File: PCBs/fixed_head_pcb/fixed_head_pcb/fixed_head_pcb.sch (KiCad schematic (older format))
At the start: 2 parts, among them J1 DB15_Female_HighDensity, U1 Pick_and_place_pcb

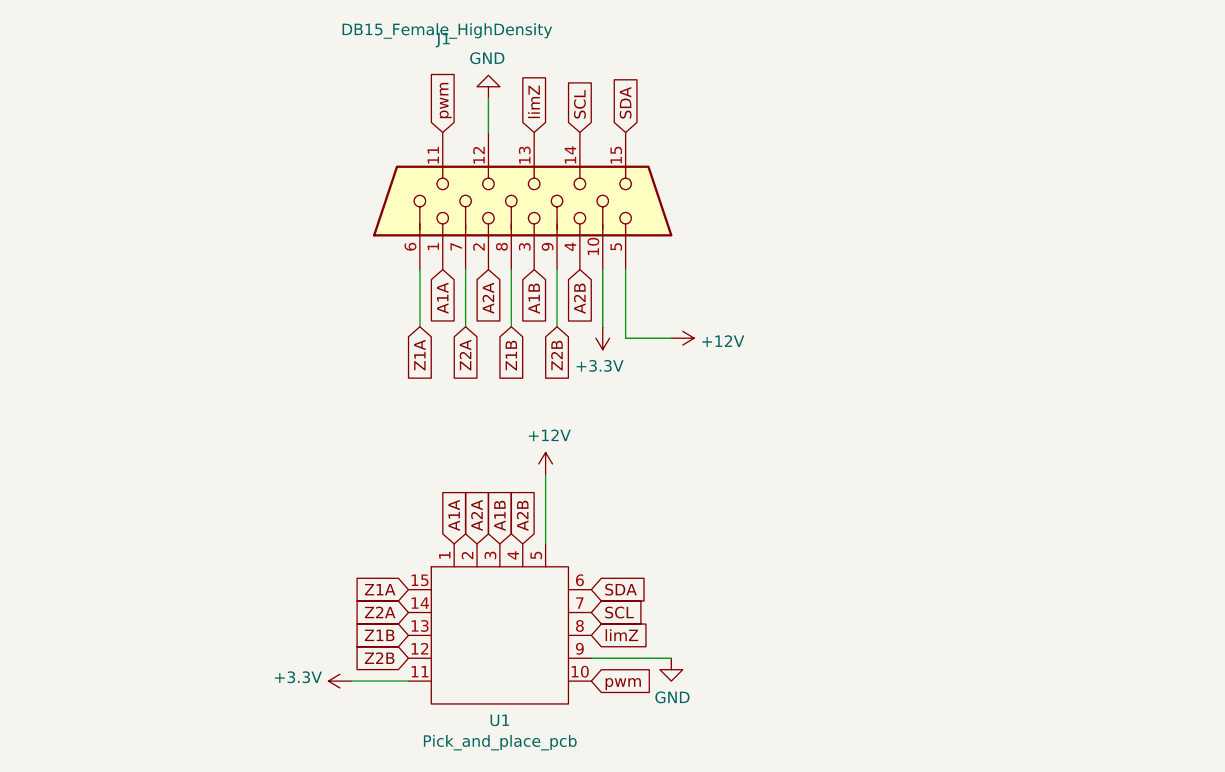
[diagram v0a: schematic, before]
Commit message: add acrylic cut and other freecad design
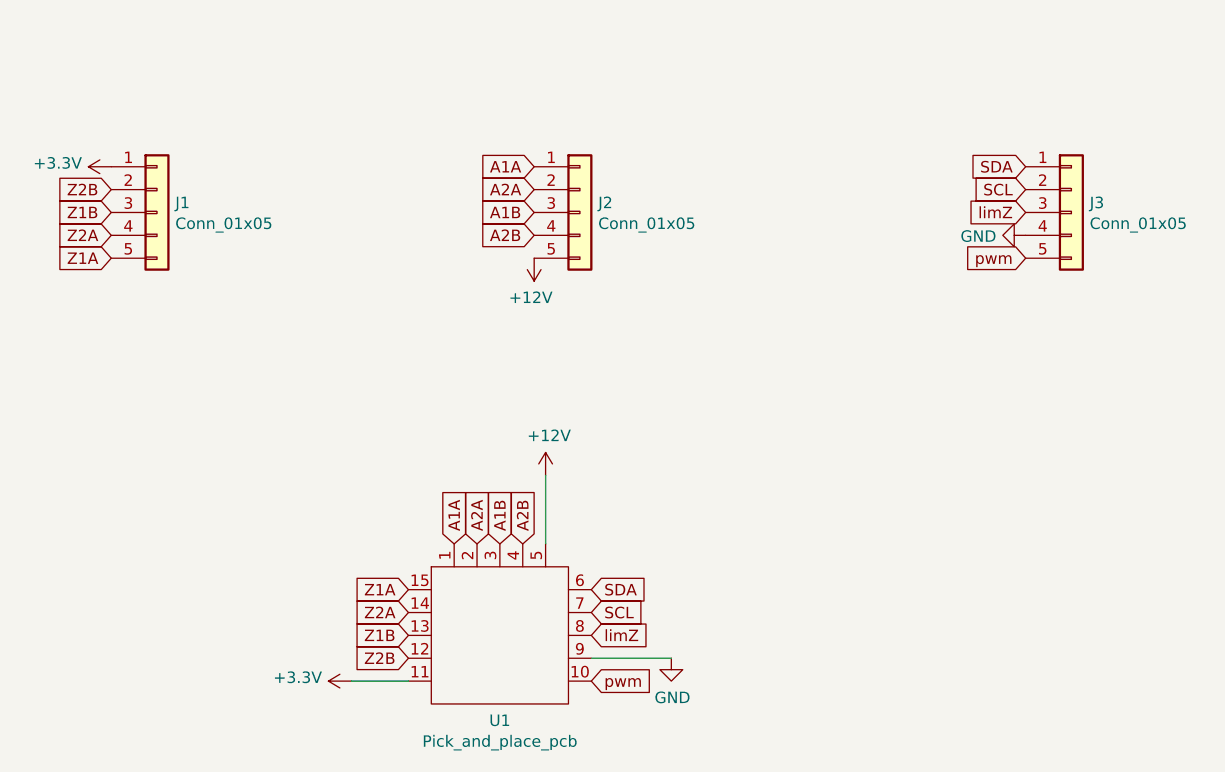
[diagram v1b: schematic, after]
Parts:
- removed J1: DB15_Female_HighDensity, Connector_Dsub:DSUB-15-HD_Female_Horizontal_P2.29x1.98mm_EdgePinOffset3.03mm_Housed_MountingHolesOffset4.94mm, symbol Connector:DB15_Female_HighDensity
- added J1, J2, J3: Conn_01x05, Connector_JST:JST_EH_B5B-EH-A_1x05_P2.50mm_Vertical, symbol Connector_Generic:Conn_01x05
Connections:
- net +12V: now also J2.5 (Pin_5)
- net +3V3: now also J1.1 (Pin_1)
- net A1A: now also J2.1 (Pin_1)
- net A1B: now also J2.3 (Pin_3)
- net A2A: now also J2.2 (Pin_2)
- net A2B: now also J2.4 (Pin_4)
- net GND: now also J3.4 (Pin_4)
- net SCL: now also J3.2 (Pin_2)
- net SDA: now also J3.1 (Pin_1)
- net Z1A: now also J1.5 (Pin_5)
- net Z1B: now also J1.3 (Pin_3)
- net Z2A: now also J1.4 (Pin_4)
- net Z2B: now also J1.2 (Pin_2)
- net limZ: now also J3.3 (Pin_3)
- net pwm: now also J3.5 (Pin_5)
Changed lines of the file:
@@
 $EndComp
 $Comp
-L Connector:DB15_Female_HighDensity J1
-U 1 1 62070157
-P 5550 2000
-F 0 "J1" V 6259 2395 50  0000 C CNN
-F 1 "DB15_Female_HighDensity" V 6299 2382 50  0000 C CNN
-F 2 "Connector_Dsub:DSUB-15-HD_Female_Horizontal_P2.29x1.98mm_EdgePinOffset3.03mm_Housed_MountingHolesOffset4.94mm" H 4600 2400 50  0001 C CNN
-F 3 " ~" H 4600 2400 50  0001 C CNN
-	1    5550 2000
+L Connector_Generic:Conn_01x05 J1
+U 1 1 62279E99
+P 3900 2050
+F 0 "J1" H 3980 2092 50  0000 L CNN
+F 1 "Conn_01x05" H 3980 2001 50  0000 L CNN
+F 2 "Connector_JST:JST_EH_B5B-EH-A_1x05_P2.50mm_Vertical" H 3900 2050 50  0001 C CNN
+F 3 "~" H 3900 2050 50  0001 C CNN
+	1    3900 2050
+	1    0    0    -1
+$EndComp
+$Comp
+L Connector_Generic:Conn_01x05 J2
+U 1 1 6227BEE4
+P 5750 2050
+F 0 "J2" H 5830 2092 50  0000 L CNN
+F 1 "Conn_01x05" H 5830 2001 50  0000 L CNN
+F 2 "Connector_JST:JST_EH_B5B-EH-A_1x05_P2.50mm_Vertical" H 5750 2050 50  0001 C CNN
+F 3 "~" H 5750 2050 50  0001 C CNN
+	1    5750 2050
+	1    0    0    -1
+$EndComp
+$Comp
+L Connector_Generic:Conn_01x05 J3
+U 1 1 6227CC03
+P 7900 2050
+F 0 "J3" H 7980 2092 50  0000 L CNN
+F 1 "Conn_01x05" H 7980 2001 50  0000 L CNN
+F 2 "Connector_JST:JST_EH_B5B-EH-A_1x05_P2.50mm_Vertical" H 7900 2050 50  0001 C CNN
+F 3 "~" H 7900 2050 50  0001 C CNN
+	1    7900 2050
+	1    0    0    -1
+$EndComp
+Text GLabel 3700 2250 0    50   Input ~ 0
+Z1A
+Text GLabel 3700 2150 0    50   Input ~ 0
+Z2A
+Text GLabel 3700 2050 0    50   Input ~ 0
+Z1B
+Text GLabel 3700 1950 0    50   Input ~ 0
+Z2B
+$Comp
+L power:+3.3V #PWR0104
+U 1 1 6227FF02
+P 3700 1850
+F 0 "#PWR0104" H 3700 1700 50  0001 C CNN
+F 1 "+3.3V" V 3715 1978 50  0000 L CNN
+F 2 "" H 3700 1850 50  0001 C CNN
+F 3 "" H 3700 1850 50  0001 C CNN
+	1    3700 1850
 	0    -1   -1   0
 $EndComp
-Text GLabel 5150 2300 3    50   Input ~ 0
+Text GLabel 5550 1850 0    50   Input ~ 0
 A1A
-Text GLabel 5350 2300 3    50   Input ~ 0
+Text GLabel 5550 1950 0    50   Input ~ 0
 A2A
-Text GLabel 5550 2300 3    50   Input ~ 0
+Text GLabel 5550 2050 0    50   Input ~ 0
 A1B
-Text GLabel 5750 2300 3    50   Input ~ 0
+Text GLabel 5550 2150 0    50   Input ~ 0
 A2B
-Wire Wire Line
-	5950 2300 5950 2600
-Wire Wire Line
-	5950 2600 6150 2600
 $Comp
-L power:+12V #PWR0104
-U 1 1 62080E1E
-P 6150 2600
-F 0 "#PWR0104" H 6150 2450 50  0001 C CNN
-F 1 "+12V" V 6165 2728 50  0000 L CNN
-F 2 "" H 6150 2600 50  0001 C CNN
-F 3 "" H 6150 2600 50  0001 C CNN
-	1    6150 2600
+L power:+12V #PWR0105
+U 1 1 62282B39
+P 5550 2250
+F 0 "#PWR0105" H 5550 2100 50  0001 C CNN
+F 1 "+12V" H 5565 2423 50  0000 C CNN
+F 2 "" H 5550 2250 50  0001 C CNN
+F 3 "" H 5550 2250 50  0001 C CNN
+	1    5550 2250
+	-1   0    0    1
+$EndComp
+Text GLabel 7700 2250 0    50   Input ~ 0
+pwm
+Text GLabel 7700 1950 0    50   Input ~ 0
+SCL
+Text GLabel 7700 1850 0    50   Input ~ 0
+SDA
+Text GLabel 7700 2050 0    50   Input ~ 0
+limZ
+$Comp
+L power:GND #PWR0106
+U 1 1 6228319E
+P 7700 2150
+F 0 "#PWR0106" H 7700 1900 50  0001 C CNN
+F 1 "GND" V 7705 2022 50  0000 R CNN
+F 2 "" H 7700 2150 50  0001 C CNN
+F 3 "" H 7700 2150 50  0001 C CNN
+	1    7700 2150
 	0    1    1    0
 $EndComp
-Wire Wire Line
-	5050 2300 5050 2550
-Wire Wire Line
-	5250 2300 5250 2550
-Wire Wire Line
-	5450 2300 5450 2550
-Wire Wire Line
-	5650 2300 5650 2550
-Wire Wire Line
-	5850 2300 5850 2550
-Text GLabel 5050 2550 3    50   Input ~ 0
-Z1A
-Text GLabel 5250 2550 3    50   Input ~ 0
-Z2A
-Text GLabel 5450 2550 3    50   Input ~ 0
-Z1B
-Text GLabel 5650 2550 3    50   Input ~ 0
-Z2B
-$Comp
-L power:+3.3V #PWR0105
-U 1 1 620828CC
-P 5850 2550
-F 0 "#PWR0105" H 5850 2400 50  0001 C CNN
-F 1 "+3.3V" H 5865 2723 50  0000 C CNN
-F 2 "" H 5850 2550 50  0001 C CNN
-F 3 "" H 5850 2550 50  0001 C CNN
-	1    5850 2550
-	-1   0    0    1
-$EndComp
-Text GLabel 5950 1700 1    50   Input ~ 0
-SDA
-Text GLabel 5750 1700 1    50   Input ~ 0
-SCL
-Text GLabel 5550 1700 1    50   Input ~ 0
-limZ
-Wire Wire Line
-	5350 1700 5350 1550
-$Comp
-L power:GND #PWR0106
-U 1 1 62084F8E
-P 5350 1550
-F 0 "#PWR0106" H 5350 1300 50  0001 C CNN
-F 1 "GND" H 5355 1377 50  0000 C CNN
-F 2 "" H 5350 1550 50  0001 C CNN
-F 3 "" H 5350 1550 50  0001 C CNN
-	1    5350 1550
-	-1   0    0    1
-$EndComp
-Text GLabel 5150 1700 1    50   Input ~ 0
-pwm
 $EndSCHEMATC
